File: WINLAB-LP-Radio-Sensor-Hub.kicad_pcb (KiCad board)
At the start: 2 copper layers, 69 parts, among them IC1 TLV74033PDBVR, J1 FTSH-105-01-L-DV-K-A, J2 Conn_Coaxial, J3 Conn_Coaxial, J4 USB_C_Receptacle_USB2.0_16P, J5 Conn_01x05, J6 Conn_01x05, J7 Conn_01x05, J8 Conn_01x05, Q1 AO3401A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

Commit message: minor schematic changes
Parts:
- added C29: 100n, Capacitor_SMD:C_0603_1608Metric_Pad1.08x0.95mm_HandSolder, F.Cu at (173.9, 125.0)
- C21, C27, C28: footprint Capacitor_SMD:C_0805_2012Metric_Pad1.18x1.45mm_HandSolder -> Capacitor_SMD:C_0603_1608Metric_Pad1.08x0.95mm_HandSolder
- moved C21 60.3 mm to (167.5, 125.0)
- moved C27 60.1 mm to (167.5, 127.5)
- moved C28 59.9 mm to (167.5, 130.0)
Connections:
- C27 pad 1: Net-(IC1-OUT) -> V_USB
- C28 pad 1: V_USB -> Net-(IC1-OUT)
- U1 pad 41: unconnected-(U1-EP-Pad41) -> GND
- U2 pad 1: unconnected-(U2-SDA-Pad1) -> I2C_SDA
- U2 pad 2: unconnected-(U2-GND-Pad2) -> GND
- U2 pad 5: unconnected-(U2-VDD-Pad5) -> +V_SYS
- U2 pad 6: unconnected-(U2-SCL-Pad6) -> I2C_SCL
- U2 pad 7: unconnected-(U2-PAD-Pad7) -> GND

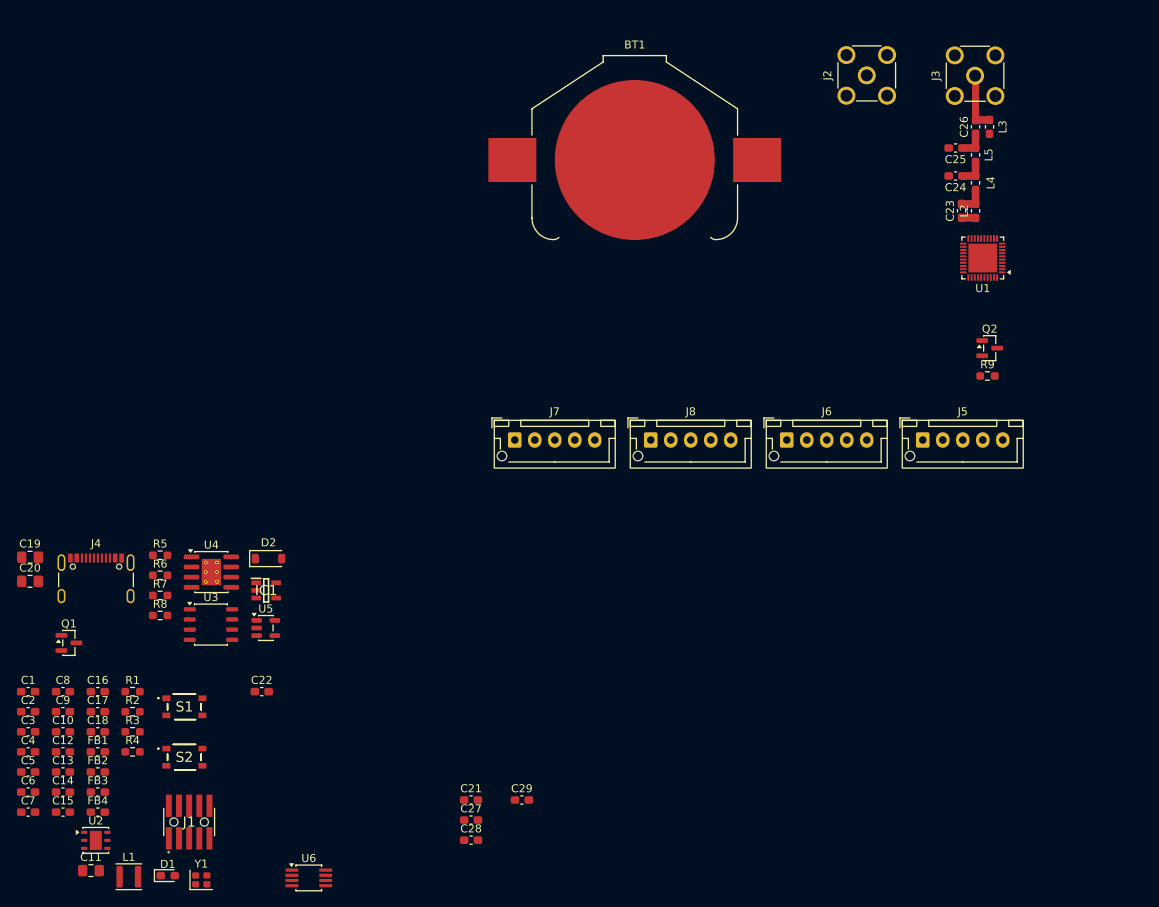
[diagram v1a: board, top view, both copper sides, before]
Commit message: initial layout and dense routing near chip
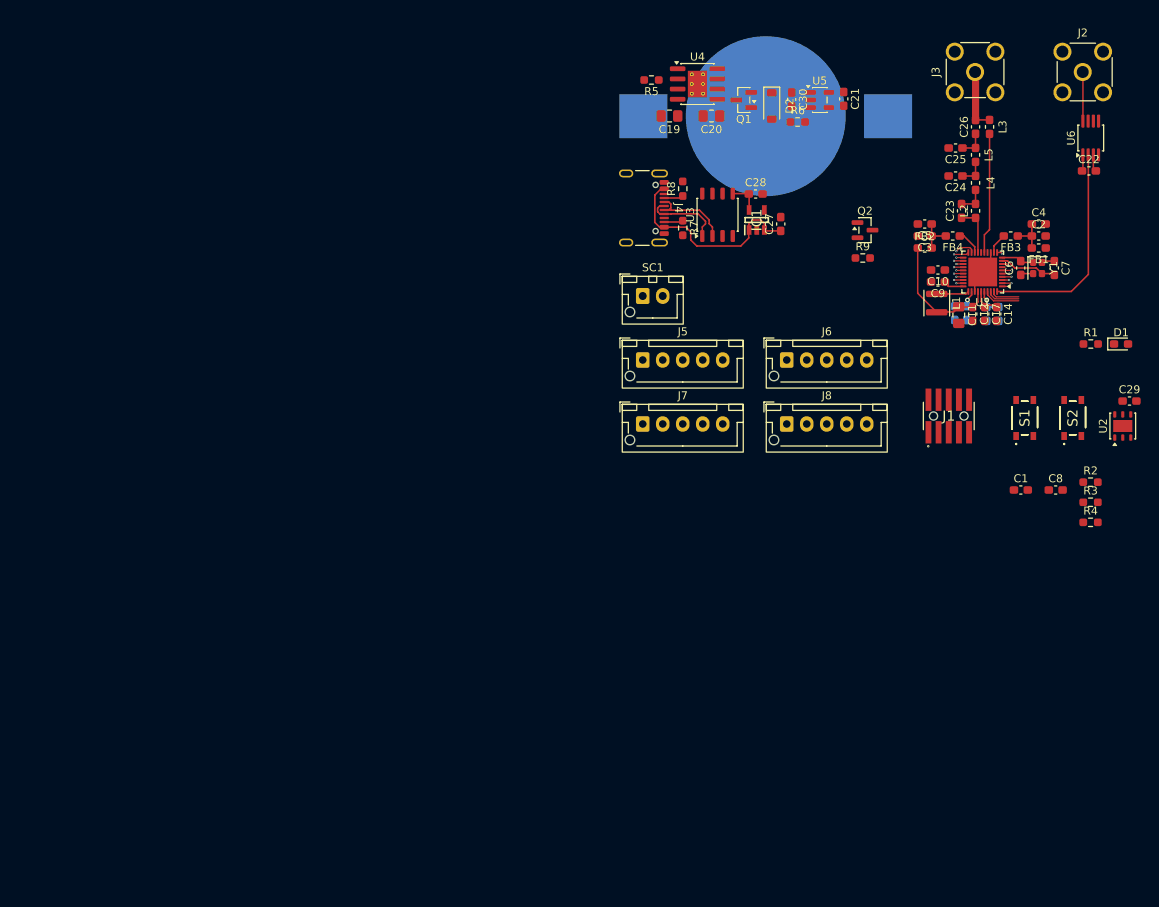
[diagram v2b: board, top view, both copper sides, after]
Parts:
- added C30: 1u, Capacitor_SMD:C_0603_1608Metric_Pad1.08x0.95mm_HandSolder, F.Cu at (207.6, 37.4)
- added SC1: Solar_Cells, Connector_JST:JST_XH_B2B-XH-AM_1x02_P2.50mm_Vertical, F.Cu at (189.0, 62.0)
- BT1, C13, C15, C16, C18: moved to B.Cu
- moved C7 145.2 mm to (240.4, 58.5), turned to -90 degrees
- moved C4 142.5 mm to (238.5, 53.0)
- moved C6 140.3 mm to (236.2, 58.5), turned to 90 degrees
- moved C2 139.6 mm to (238.5, 54.5)
- moved U2 138.4 mm to (249.0, 78.2), turned to 90 degrees
- moved D1 136.4 mm to (248.8, 68.0)
- moved U6 134.6 mm to (245.0, 42.2), turned to 90 degrees
- moved FB3 133.6 mm to (235.0, 54.5), turned to 180 degrees
- moved FB1 133.4 mm to (238.5, 56.0), turned to 180 degrees
- moved C5 131.3 mm to (224.2, 53.0), turned to 180 degrees
- moved C14 131.1 mm to (233.2, 64.2), turned to -90 degrees
- moved C13 130.2 mm to (233.5, 64.2), turned to -90 degrees
- moved Y1 129.5 mm to (238.3, 58.5), turned to -90 degrees
- moved C15 129.1 mm to (229.5, 64.1), turned to -90 degrees
- moved FB4 128.9 mm to (227.8, 54.5), turned to 180 degrees
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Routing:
- net BACKSCATTER_PULSE: track 0.00 -> 27.2 mm
- net V_USB: track 0.00 -> 25.9 mm
- net EFR32_DCDC: track 0.00 -> 15.3 mm
- net RF_I: track 0.00 -> 15.1 mm
- net +V_SYS: track 0.00 -> 12.3 mm, vias 0 -> 2
- net GND: track 0.00 -> 11.1 mm
- net USB-: track 0.00 -> 10.7 mm
- net USB+: track 0.00 -> 9.91 mm
- net Net-(U1-HFXTAL_I): track 0.00 -> 7.24 mm
- net Net-(J2-In): track 0.00 -> 6.15 mm
- net Net-(C3-Pad1): track 0.00 -> 4.77 mm
- net Net-(C2-Pad1): track 0.00 -> 4.77 mm
- net ~{SENSOR_ENABLE}: track 0.00 -> 4.62 mm
- net RF_O: track 1.76 -> 6.20 mm
- net VCOM_RX: track 0.00 -> 4.12 mm
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
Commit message: more layout and routing work
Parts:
- moved R2 67.9 mm to (196.5, 37.7), turned to -90 degrees
- moved R4 67.5 mm to (196.6, 43.2), turned to -90 degrees
- moved R3 66.0 mm to (200.0, 39.5), turned to 90 degrees
- moved D1 63.7 mm to (189.0, 46.0), turned to 90 degrees
- moved S2 63.3 mm to (190.5, 41.5), turned to 180 degrees
- moved C1 63.2 mm to (198.2, 35.8), turned to -90 degrees
- moved S1 62.0 mm to (190.5, 36.0), turned to 180 degrees
- moved C8 61.8 mm to (198.2, 41.2), turned to -90 degrees
- moved R1 58.3 mm to (191.0, 46.0), turned to 90 degrees
- moved SC1 25.9 mm to (214.5, 57.5)
- moved R5 23.2 mm to (208.0, 49.8), turned to 0 degrees
- moved C19 21.6 mm to (212.0, 48.5), turned to -90 degrees
- moved U4 15.4 mm to (208.0, 45.0), turned to 90 degrees
- moved C20 14.9 mm to (212.0, 43.2), turned to -90 degrees
- moved Q2 14.8 mm to (204.5, 62.0), turned to 180 degrees
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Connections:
- J1 pad 4: DBG_UART_RX -> VCOM_RX
- J1 pad 5: DBG_UART_TX -> VCOM_TX
- R2 pad 1: Net-(S1-NO_1) -> Net-(S1-COM_1)
- R4 pad 1: Net-(S2-NO_1) -> Net-(S2-COM_1)
- S1 pad 1: RESET -> Net-(S1-COM_1)
- S1 pad 2: RESET -> Net-(S1-COM_1)
- S1 pad 3: Net-(S1-NO_1) -> RESET
- S1 pad 4: Net-(S1-NO_1) -> RESET
- S2 pad 1: BTN_USR -> Net-(S2-COM_1)
- S2 pad 2: BTN_USR -> Net-(S2-COM_1)
- S2 pad 3: Net-(S2-NO_1) -> BTN_USR
- S2 pad 4: Net-(S2-NO_1) -> BTN_USR
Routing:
- net GND: track 11.1 -> 278.8 mm, vias 0 -> 13
- net +V_SYS: track 12.3 -> 115.8 mm, vias 2 -> 6
- net RESET: track 0.66 -> 66.6 mm, vias 1 -> 2
- net BTN_USR: track 2.57 -> 60.6 mm, vias 1 -> 2
- net IO2_0: track 0.86 -> 50.3 mm, vias 1 -> 2
- net IO2_1: track 1.16 -> 49.5 mm, vias 1 -> 2
- net IO2_2: track 0.86 -> 48.4 mm, vias 1 -> 2
- net +V_SENSOR: track 0.00 -> 42.1 mm
- net LED_USR: track 1.90 -> 43.8 mm, vias 1 -> 2
- net IO0_0: track 0.86 -> 36.7 mm
- net IO3_0: track 1.16 -> 36.7 mm, vias 1 -> 2
- net IO3_1: track 0.86 -> 35.3 mm, vias 1 -> 2
- net ~{SENSOR_ENABLE}: track 4.62 -> 38.2 mm, vias 0 -> 2
- net IO3_2: track 1.16 -> 34.2 mm, vias 1 -> 2
- net IO0_1: track 0.86 -> 33.5 mm
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- added copper zone on B.Cu, net GND
- added copper zone on F.Cu, net GND
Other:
- board outline added: 65 x 53 mm
- board text added: "PB0"
- board text added: "PB1"
- board text added: "RESET"

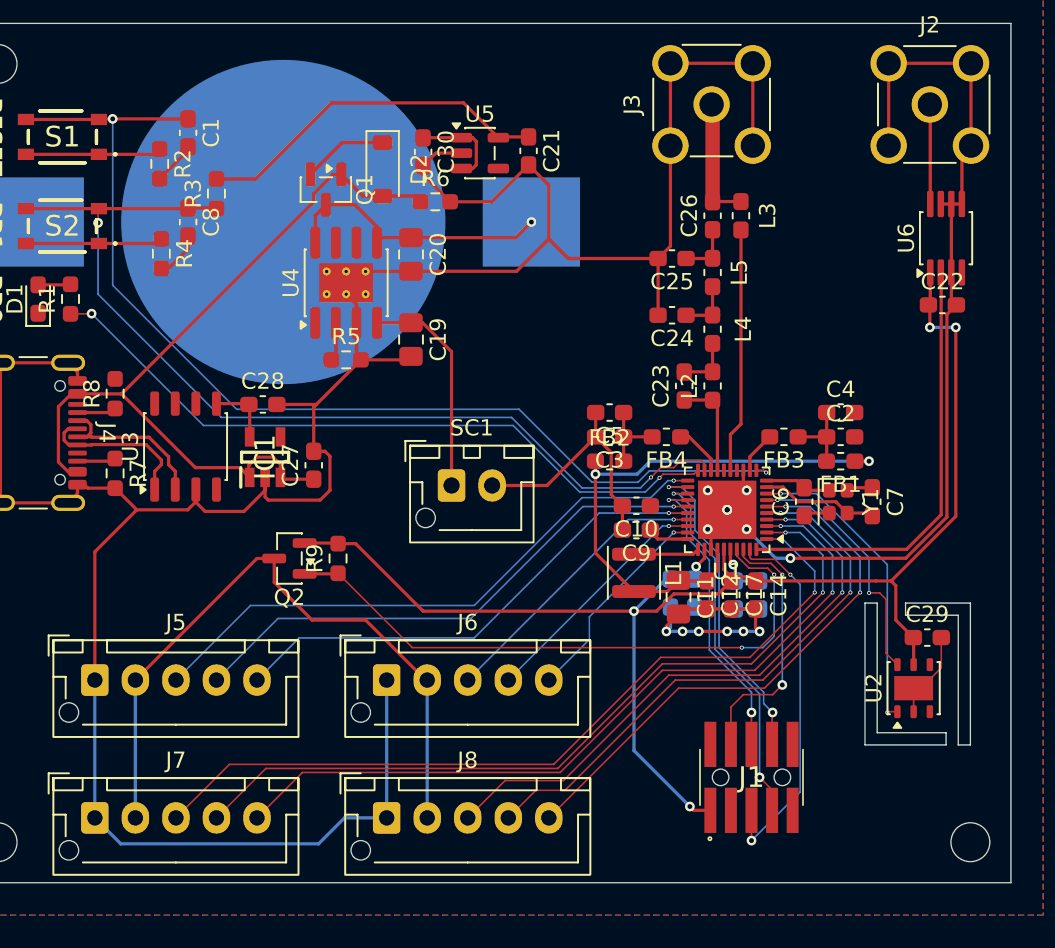
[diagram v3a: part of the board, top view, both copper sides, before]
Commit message: minor layout tweaks, add external power header
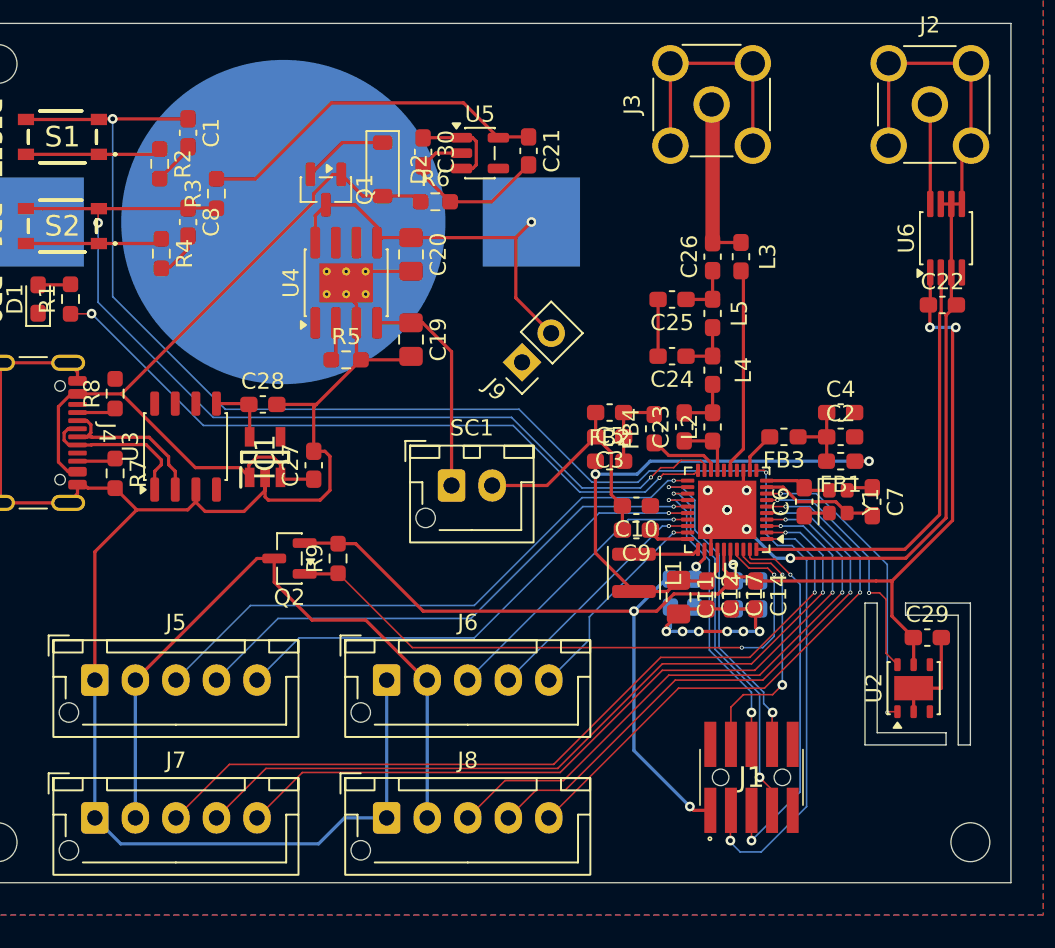
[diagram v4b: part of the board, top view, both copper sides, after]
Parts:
- added J9: Conn_01x02, Connector_PinHeader_2.54mm:PinHeader_1x02_P2.54mm_Vertical, F.Cu at (218.8, 49.9)
- moved C23 2.52 mm to (228.8, 53.9)
- moved C24 2.52 mm to (228.1, 49.5)
- moved C25 2.52 mm to (228.1, 46.0)
- moved C26 2.52 mm to (230.6, 43.4)
- moved L2 2.52 mm to (230.6, 53.9)
- moved L3 2.52 mm to (232.3, 43.4)
- moved L4 2.52 mm to (230.6, 50.4)
- moved L5 2.52 mm to (230.6, 46.9)
- moved FB4 0.90 mm to (227.0, 54.0), turned to 90 degrees
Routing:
- net RESET: track 66.6 -> 97.3 mm, vias 2 -> 3
- net GND: track 278.8 -> 250.6 mm
- net V_BAT: track 17.4 -> 24.1 mm
- net RF_O: track 6.20 -> 3.66 mm
- net Net-(J3-In): track 7.78 -> 10.3 mm
- net RF_I: track 15.1 -> 12.7 mm
- net Net-(U1-PAVDD): track 3.15 -> 4.47 mm
